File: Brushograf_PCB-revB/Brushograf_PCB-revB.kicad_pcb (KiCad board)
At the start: 2 copper layers, 100 x 151.1 mm, 72 parts, among them J1 Conn_01x05_Socket, J12 USB-C PD in, J13 Pendant, J2 Conn_01x05_Socket, J3 Conn_01x05_Socket, J8 SD_CARD_MICRO_AMPHENOL_114008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, SW1 ESP POWER, SW2 SW_Lever_1P2T_NKK_GW12LxH, U1 ULN2003A, U2 ULN2003A, U3 ULN2003A, U4 ESP32-DevKitC, U6 CH224K, U7 TPS54202, U8 TPS54202

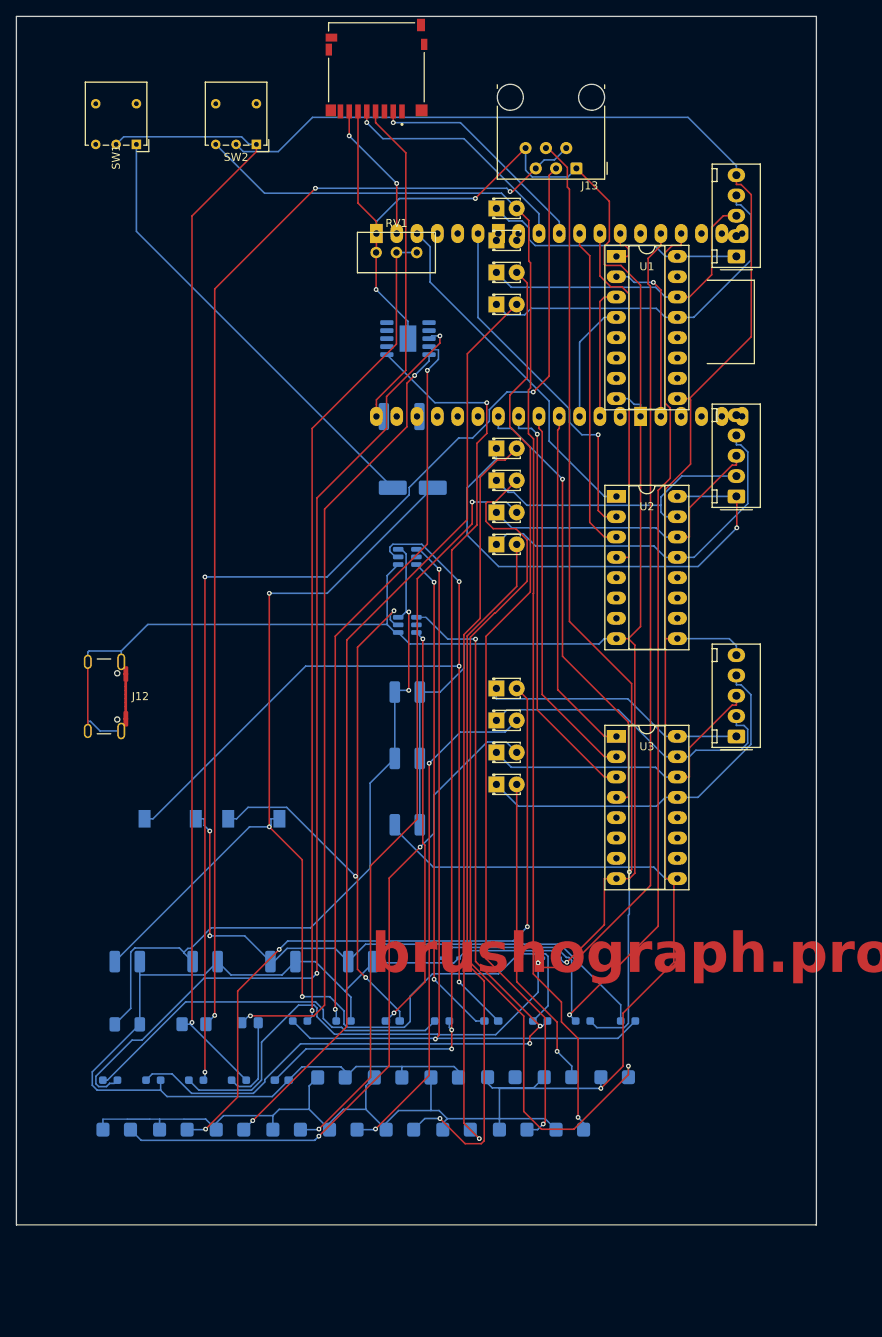
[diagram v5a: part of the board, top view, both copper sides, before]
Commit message: Diagonal stretch outline, labeled axes, fix J12, isolate U4
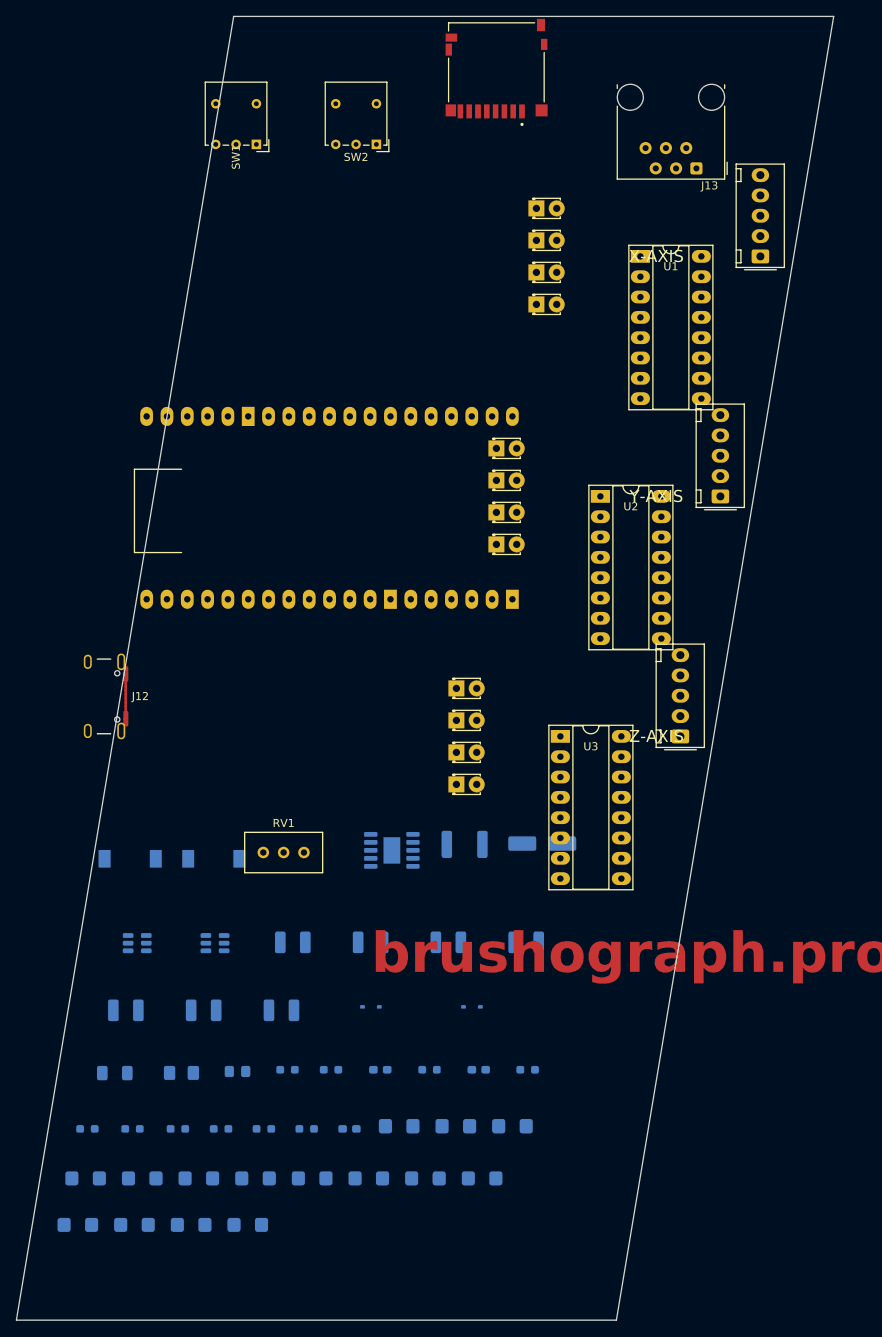
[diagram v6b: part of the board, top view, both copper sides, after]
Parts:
- moved RV1 76.3 mm to (45.9, 114.5)
- moved U6 64.0 mm to (56.9, 114.2)
- moved R26 63.4 mm to (24.5, 149.1)
- moved R31 63.4 mm to (18.9, 149.1)
- moved U7 58.9 mm to (25.1, 125.8)
- moved F1 54.1 mm to (66.0, 113.5)
- moved R2 53.5 mm to (18.6, 155.2)
- moved R12 53.5 mm to (25.7, 155.2)
- moved R6 53.5 mm to (32.8, 155.2)
- moved C17 49.9 mm to (73.7, 125.7)
- moved D14 47.3 mm to (75.7, 113.4)
- moved U8 46.5 mm to (34.8, 125.8)
- moved R1 42.0 mm to (38.9, 161.1)
- moved R8 42.0 mm to (17.7, 161.1)
- moved R3 42.0 mm to (31.8, 161.1)
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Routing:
- net GND: track 436.8 -> 0.00 mm, vias 3 -> 0
- net 5V: track 354.8 -> 0.00 mm, vias 1 -> 0
- net PEND_TX: track 161.0 -> 0.00 mm, vias 1 -> 0
- net Net-(D1-A): track 159.8 -> 0.00 mm, vias 1 -> 0
- net 5V_LOGIC: track 154.4 -> 0.00 mm, vias 3 -> 0
- net PEND_TX_CON: track 144.1 -> 0.00 mm, vias 3 -> 0
- net PEND_5V: track 143.9 -> 0.00 mm, vias 3 -> 0
- net 5V_SYS: track 142.6 -> 0.00 mm, vias 1 -> 0
- net PEND_RX: track 130.1 -> 0.00 mm, vias 1 -> 0
- net Net-(U6-VBUS): track 124.6 -> 0.00 mm, vias 2 -> 0
- net Net-(U6-VDD): track 122.5 -> 0.00 mm, vias 3 -> 0
- net PEND_RX_CON: track 119.5 -> 0.00 mm, vias 1 -> 0
- net Net-(D4-A): track 117.3 -> 0.00 mm, vias 1 -> 0
- net Net-(U7-SW): track 116.8 -> 0.00 mm, vias 3 -> 0
- net Net-(D3-A): track 116.8 -> 0.00 mm, vias 1 -> 0
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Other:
- board size 100 x 151.1 mm -> 102.2 x 163 mm
- board text added: "X-AXIS"
- board text added: "Y-AXIS"
- board text added: "Z-AXIS"

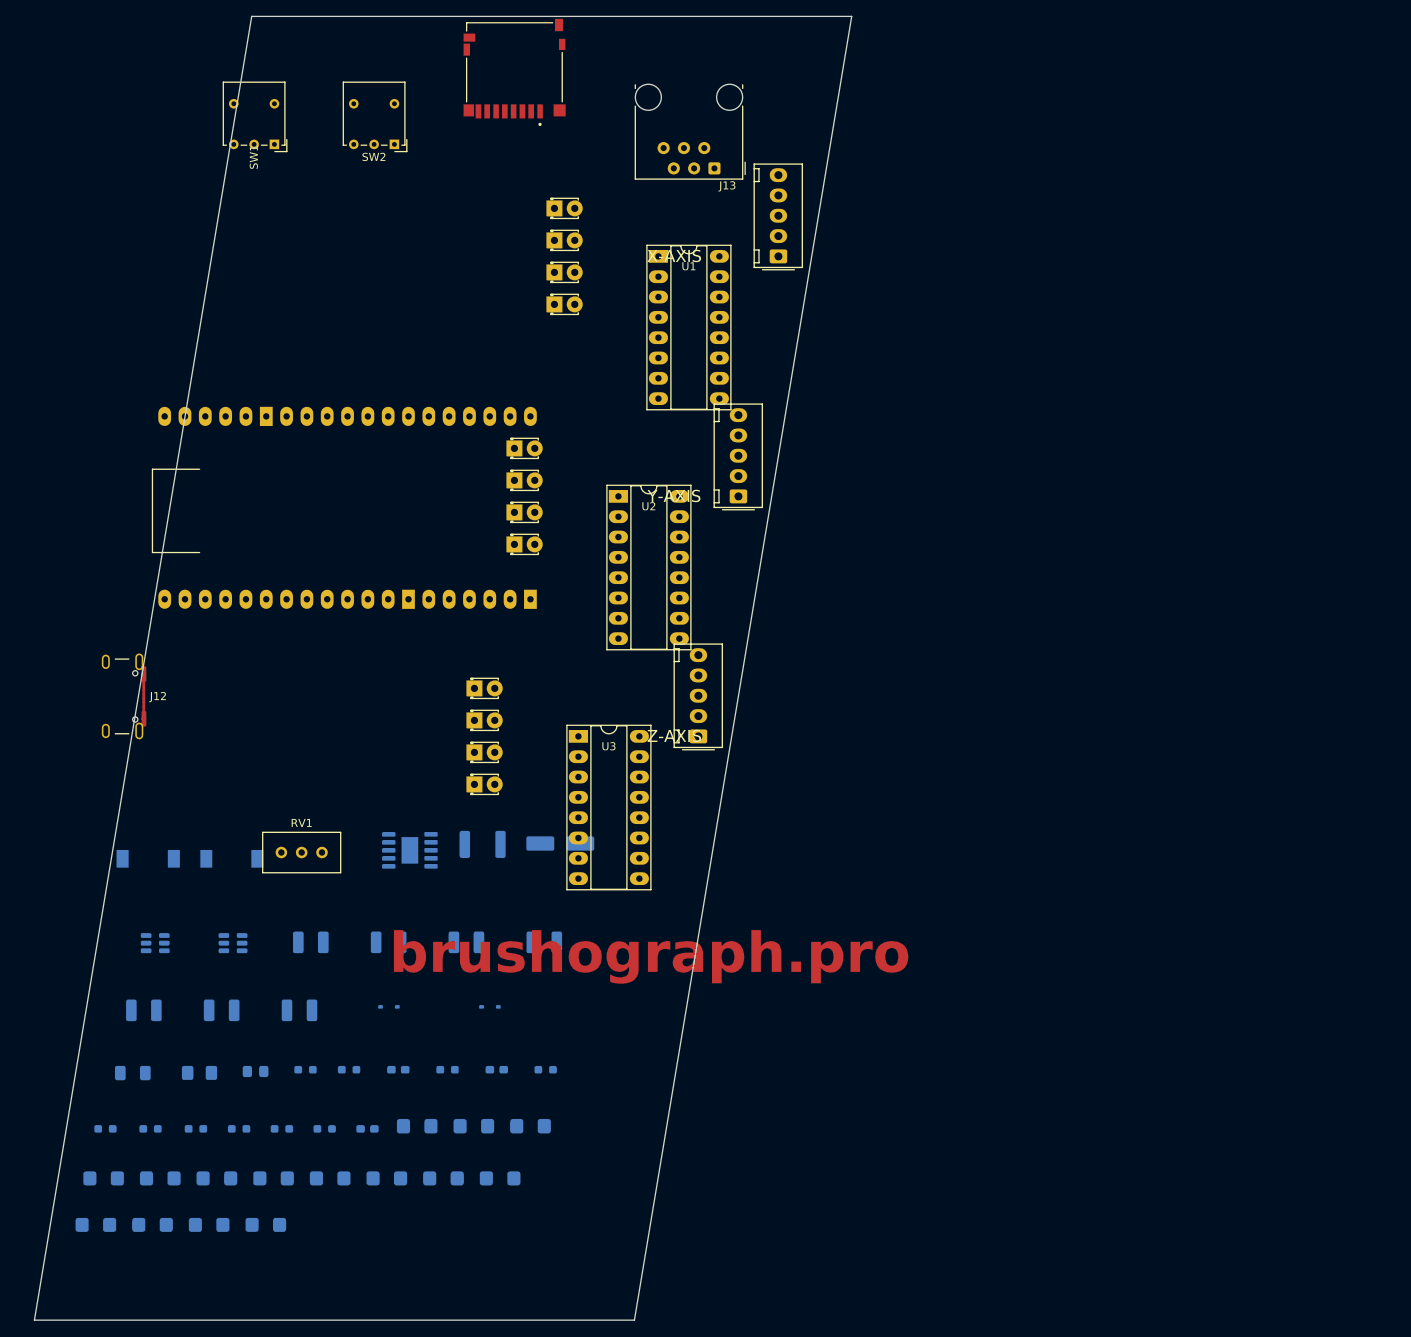
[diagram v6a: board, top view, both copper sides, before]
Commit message: Lengthwise board stretch, labeled X/Y/Z, refined J12/U4 left edge
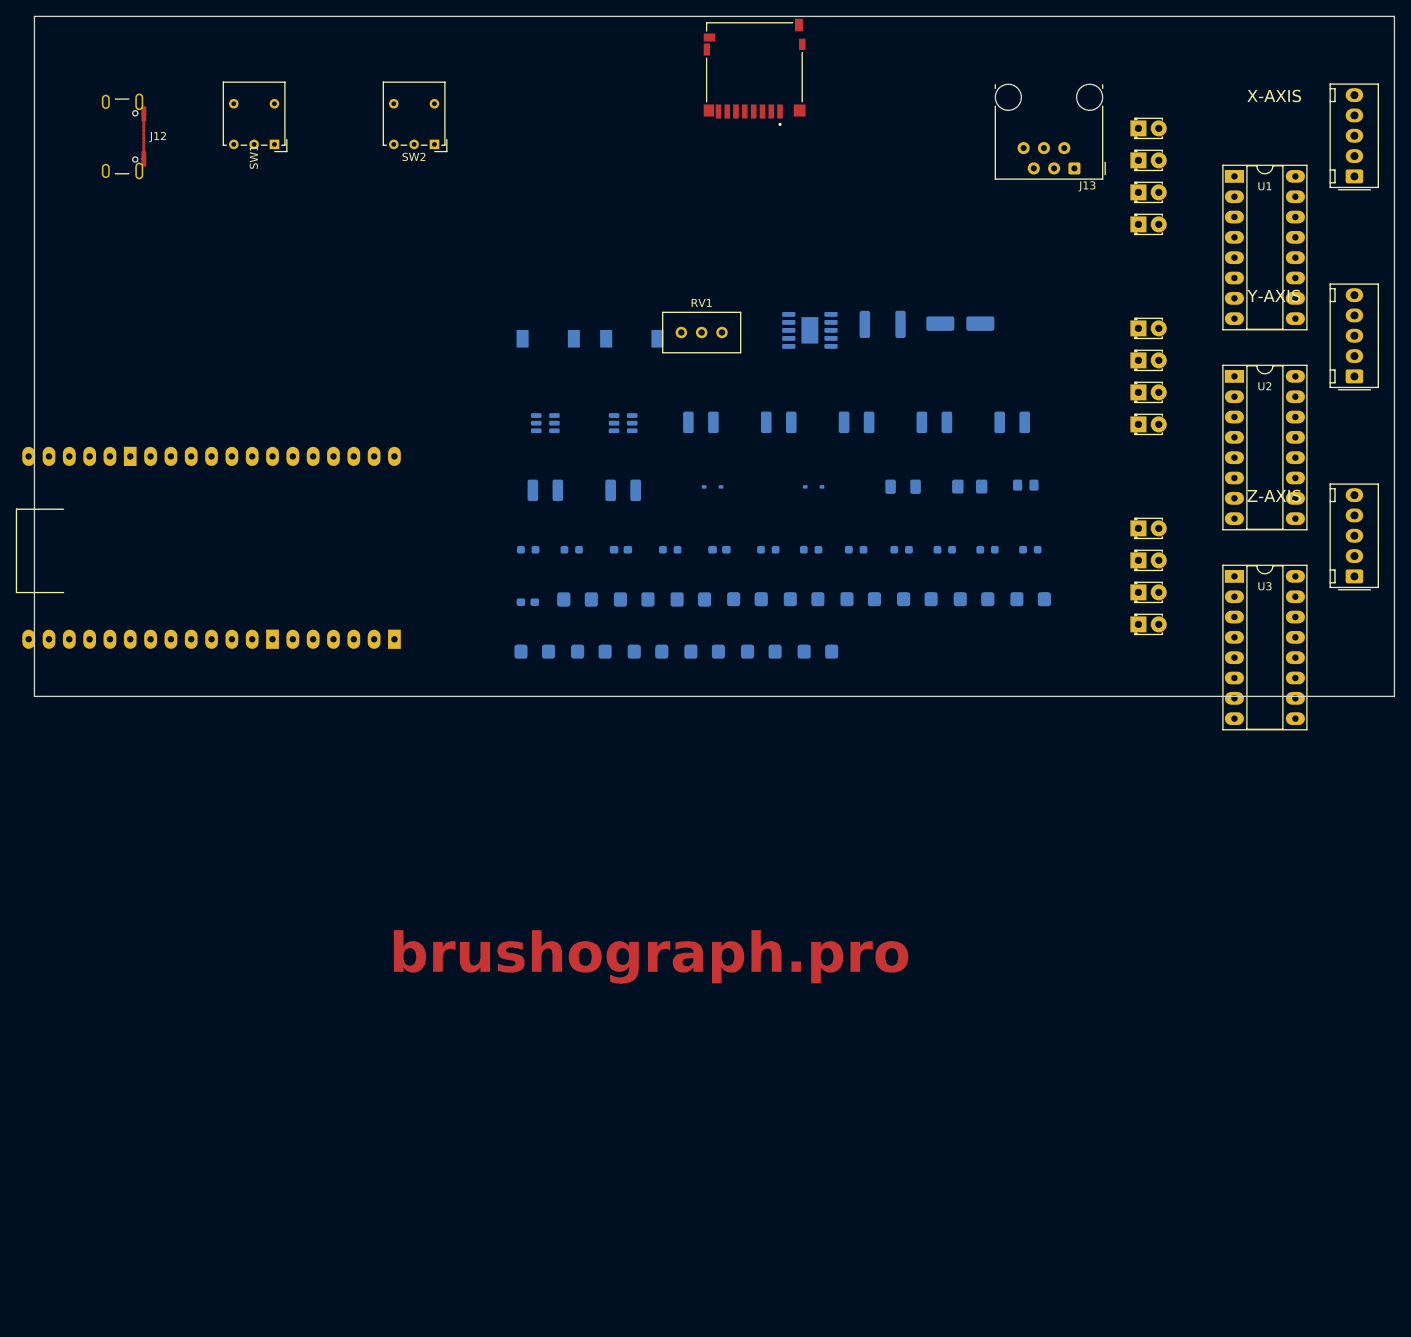
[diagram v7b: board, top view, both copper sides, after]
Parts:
- moved C15 131.1 mm to (132.2, 60.7)
- moved D17 121.0 mm to (133.9, 68.6)
- moved F2 121.0 mm to (126.9, 68.8)
- moved C7 121.0 mm to (118.6, 68.8)
- moved R30 114.1 mm to (129.1, 76.7)
- moved R25 114.1 mm to (134.5, 76.7)
- moved R23 114.1 mm to (118.4, 76.7)
- moved R26 114.1 mm to (112.7, 76.7)
- moved R29 114.1 mm to (123.8, 76.7)
- moved R31 114.1 mm to (107.1, 76.7)
- moved R12 108.3 mm to (106.2, 82.9)
- moved R2 108.3 mm to (99.1, 82.9)
- moved R11 108.3 mm to (120.4, 82.9)
- moved R4 108.3 mm to (134.5, 82.9)
- moved R9 108.3 mm to (127.4, 82.9)
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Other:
- board size 102.2 x 163 mm -> 170 x 85 mm
